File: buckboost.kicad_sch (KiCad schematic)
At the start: 3 parts

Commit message: buckboost: draft LM5176 4-switch power stage
Placed and wired the LM5176 (U1, HTSSOP-28-EP, LCSC C442493 per
TOPOLOGY.md) plus its support network:

Power stage: Q1..Q4 (30V/20A N-FET placeholder -- v1's FDS9926A is
undersized for v2's 5A/6.5A-peak spec, so this is marked TBD for a
proper JLCPCB Basic pick), L1 6.8uH, R8 5m current sense, boot caps
C5/C6 100nF, output caps C10/C11 22uF each.

Chip support: VIN caps C1/C2 22uF, VCC decoupling C3 2.2uF, BIAS C4
1uF, feedback R1/R2 (110k/10k -> 12.0V from LM5176's 1.0V Vref),
COMP R3 20k + C8 4.7nF, SS C7 10nF, RT R4 40.2k (~500kHz), EN
pull-up R6 100k to BAT+. MODE and DITH tied to GND.

Named nets wired: BAT+, GND, VOUT_12V, SW1, SW2, HDRV1/2, LDRV1/2,
BOOT1/2, FB, LM5176_VCC, LM5176_BIAS, SS, COMP, COMP_MID, RT, EN.
No hierarchical sheet pins -- power rails cross sheets via global
labels per the root-sheet plan.

TBD annotation on-sheet lists what needs a review pass: FET MPN,
CS/CSG hookup (currently unconnected -- either wire R8 across L1 as
high-side inductor sense OR switch to Rds(on) sensing on Q2/Q3),
SLOPE resistor R5 sizing, and optional PGOOD LED.

Also cleaned the three TEMPLATE_R/C/D placeholder symbols that
create_schematic left in all four sub-sheets.

Co-Authored-By: Claude Opus 4.7 <noreply@anthropic.com>
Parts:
- removed _TEMPLATE_C: C_TEMPLATE, symbol Device:C
- removed _TEMPLATE_D: LED_TEMPLATE, symbol Device:LED
- removed _TEMPLATE_R: R_TEMPLATE, symbol Device:R
- added C1, C10, C11, C2: 22uF, symbol Device:C
- added C3: 2.2uF, symbol Device:C
- added C4: 1uF, symbol Device:C
- added C5, C6: 100nF, symbol Device:C
- added C7: 10nF, symbol Device:C
- added C8: 4.7nF, symbol Device:C
- added L1: 6.8uH, symbol Device:L
- added Q1, Q2, Q3, Q4: 30V/20A_NFET, symbol Device:Q_NMOS
- added R1: 110k, symbol Device:R
- added R2: 10k, symbol Device:R
- added R3: 20k, symbol Device:R
- added R4: 40.2k, symbol Device:R
- added R6: 100k, symbol Device:R
- added R8: 5m, symbol Device:R
- added U1: LM5176PWP, Package_SO:HTSSOP-28-1EP_4.4x9.7mm_P0.65mm_EP2.85x5.4mm_ThermalVias, symbol Regulator_Switching:LM5176PWP
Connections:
- new net BAT+: C1.1, C1.2, C10.2, C11.2, C2.1, C2.2, C3.1, C3.2, C4.1, C4.2, C7.2, C8.2, Q1.D, Q2.S, Q3.S, R2.2, R3.1, R4.1, R4.2, R6.2, U1.10 (AGND), U1.2 (VIN), U1.22 (PGND), U1.23 (VCC), U1.24 (BIAS), U1.29 (PowerPAD), U1.3 (VISNS), U1.4 (MODE), U1.5 (DITH), U1.6 (RT/SYNC), U1.9 (COMP)
- new net BOOT1: C5.1, U1.26 (BOOT1)
- new net BOOT2: C6.1, U1.20 (BOOT2)
- new net COMP_MID: C8.1, R3.2
- new net EN: R6.1, U1.1 (EN/UVLO)
- new net FB: R1.2, R2.1, U1.11 (FB)
- new net HDRV1: Q1.G, U1.27 (HDRV1)
- new net HDRV2: Q4.G, U1.19 (HDRV2)
- new net LDRV1: Q2.G, U1.25 (LDRV1)
- new net LDRV2: Q3.G, U1.21 (LDRV2)
- new net SS: C7.1, U1.8 (SS)
- new net SW1: C5.2, L1.1, Q1.S, Q2.D, U1.28 (SW1)
- new net SW2: C6.2, L1.2, Q3.D, Q4.S, U1.18 (SW2)
- new net VOUT_12V: C10.1, C11.1, Q4.D, R1.1, U1.12 (VOSNS), U1.13 (ISNS(-)), U1.14 (ISNS(+))
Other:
- note added: "TBD - review pass needed: Q1-Q4 = 30V/20A N-FET MPN (v1's FDS9926A undersized); R8 = high-side inductor current sense (tie CS/CSG properly or use Rds(on) sensing); SLOPE (pin 7) resistor; PGOOD (pin 17) LED optional"
- note added: "buckboost — LM5176 4-switch synchronous, 12V/5A"

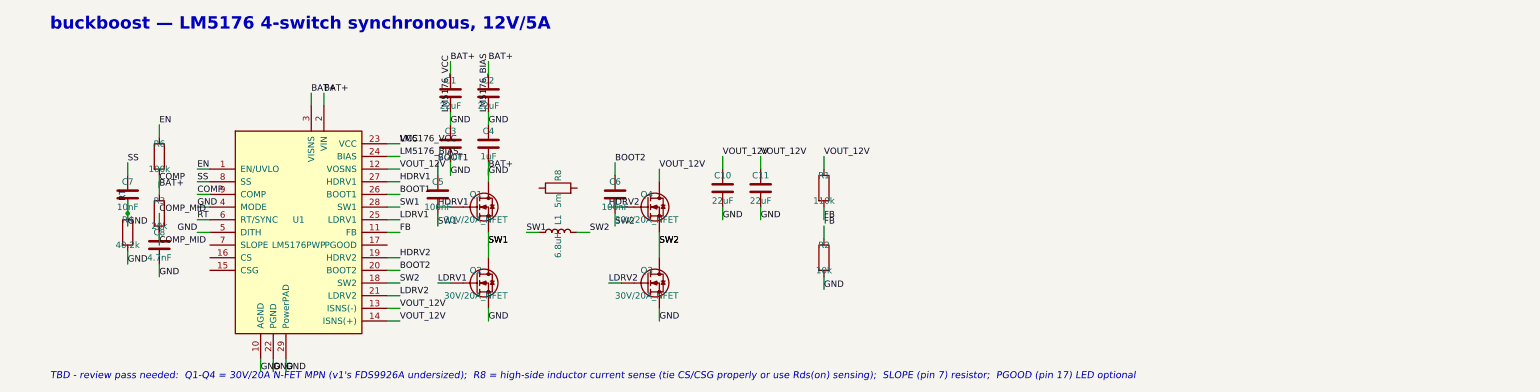
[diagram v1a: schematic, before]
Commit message: buckboost: re-space at 15.24mm grid + resolve TBDs; add bms.VSS PWR_FLAG
Nuke-and-restart of buckboost.kicad_sch. The prior draft had passives
stacked at 10 mm on the same X, which silently bridged the label stubs
between rows and merged BAT+ / GND / VCC / LM5176_VCC / LM5176_BIAS /
COMP / RT into one 31-pin mega-net (feedback_schematic_vertical_spacing).
Full-project ERC caught the resulting BAT+ ↔ GND short.

Fresh layout at 15.24 mm vertical grid per column: LM5176 center, config
resistors + timing/compensation caps on the west (R6 EN / C7 SS / R4 RT
/ R5 SLOPE in col A; R3 COMP series in col B; C8 COMP cap in col C).
Power stage on the east: Q1/Q2 buck FETs, L1 6.8 µH inductor rotated 90°,
Q3/Q4 boost FETs; C1/C2 22 µF Cin at BAT+, C3/C4 LM5176 bias/vcc bypass,
C5/C6 boot caps, C10/C11 22 µF Cout at VOUT_12V, R1/R2 FB divider.

Also resolved the yesterday-TBDs from the prior buckboost commit:
- CS/CSG: use Rds(on)-of-Q2 buck-LS sensing (CS → SW1, CSG → GND). Drops
  the R8 shunt from the BOM. Cheap; loses some accuracy but keeps the
  BOM tight. Real design pass should verify against LM5176 §9.3.11 for
  buck+boost coverage.
- SLOPE: R5 = 10 kΩ to GND (placeholder — TBD per LM5176 §9.3.7 given
  final Fsw/L1 choice).
- PGOOD (U1.17): no-connect flag added.
- MODE (U1.4): tied to GND for auto PFM/PWM (efficiency-first).
- DITH (U1.5): no-connect flag added.

PWR_FLAGs: LM5176_VCC on buckboost so ERC recognises the internal LDO
as a driven power rail; bms.VSS on the BQ76920 side for the same reason.
Sheet-level ERC clean apart from cosmetic Unspecified/Passive pin-type
warnings.

Full-project ERC now: 0 errors, 34 warnings (all cosmetic — Unspecified/
Passive type mismatches, local↔global label pairs, 2 leftover Q1-Q4
'SOIC-8' footprint links from the old draft's Value fields, 1 stray
wire endpoint).

Co-Authored-By: Claude Opus 4.7 <noreply@anthropic.com>
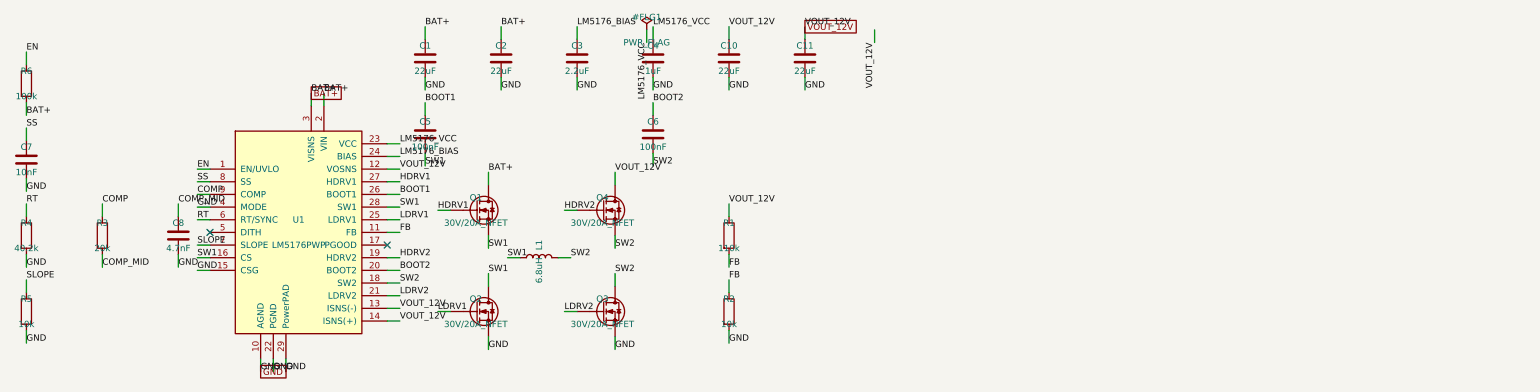
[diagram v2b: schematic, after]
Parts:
- removed R8: 5m, symbol Device:R
- added R5: 10k, symbol Device:R
- U1: footprint Package_SO:HTSSOP-28-1EP_4.4x9.7mm_P0.65mm_EP2.85x5.4mm_ThermalVias -> (none)
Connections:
- net BAT+: no longer C1.2, C10.2, C11.2, C2.2, C3.1, C3.2, C4.1, C4.2, C7.2, C8.2, Q2.S, Q3.S, R2.2, R3.1, R4.1, R4.2, U1.10 (AGND), U1.22 (PGND), U1.23 (VCC), U1.24 (BIAS), U1.29 (PowerPAD), U1.4 (MODE), U1.5 (DITH), U1.6 (RT/SYNC), U1.9 (COMP)
- net SW1: now also U1.16 (CS)
- net GND: now reaches U1.15 (CSG)
- net GND: now also C1.2, C10.2, C11.2, C2.2, C3.2, C4.2, C7.2, C8.2, Q2.S, Q3.S, R2.2, R4.2, U1.10 (AGND), U1.22 (PGND), U1.29 (PowerPAD), U1.4 (MODE), R5.2
- net SLOPE: now reaches U1.7 (SLOPE)
- net SLOPE: now also R5.1
- new net COMP: R3.1, U1.9 (COMP)
- new net LM5176_BIAS: C3.1, U1.24 (BIAS)
- new net LM5176_VCC: C4.1, U1.23 (VCC)
- new net RT: R4.1, U1.6 (RT/SYNC)
- no-connect marks 0 -> 2
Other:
- note removed: "TBD - review pass needed: Q1-Q4 = 30V/20A N-FET MPN (v1's FDS9926A undersized); R8 = high-side inductor current sense (tie CS/CSG properly or use Rds(on) sensing); SLOPE (pin 7) resistor; PGOOD (pin 17) LED optional"
- note removed: "buckboost — LM5176 4-switch synchronous, 12V/5A"
